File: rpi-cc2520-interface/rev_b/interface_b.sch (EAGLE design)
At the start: 5 parts, among them J1 PINHD-2X12/SMD, J2 PINHD-2X12/SMD

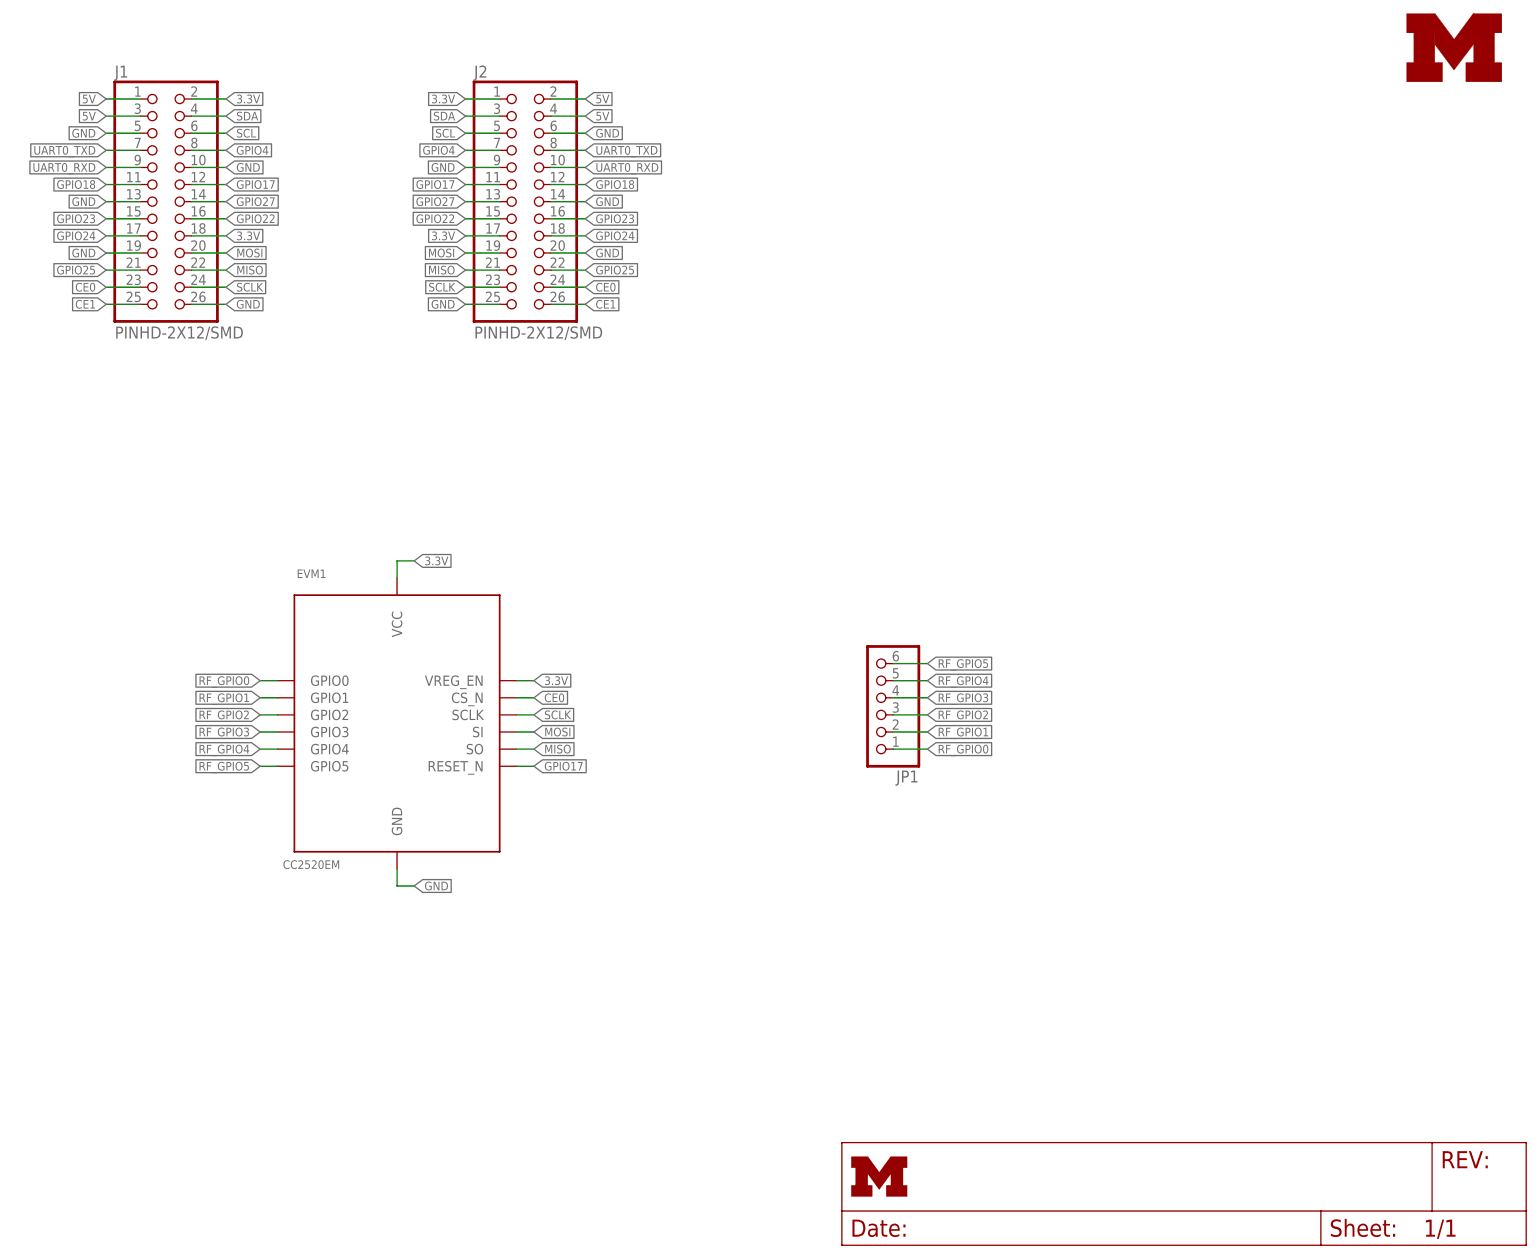
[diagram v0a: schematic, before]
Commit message: new rpi-cc2520 board is routed. want to add pin labels
git-svn-id: svn+ssh://energy.eecs.umich.edu/svnroot/shed/projects/pi-router/eagle@2756 d5a83394-2863-40c7-9603-03341d4c7fdc
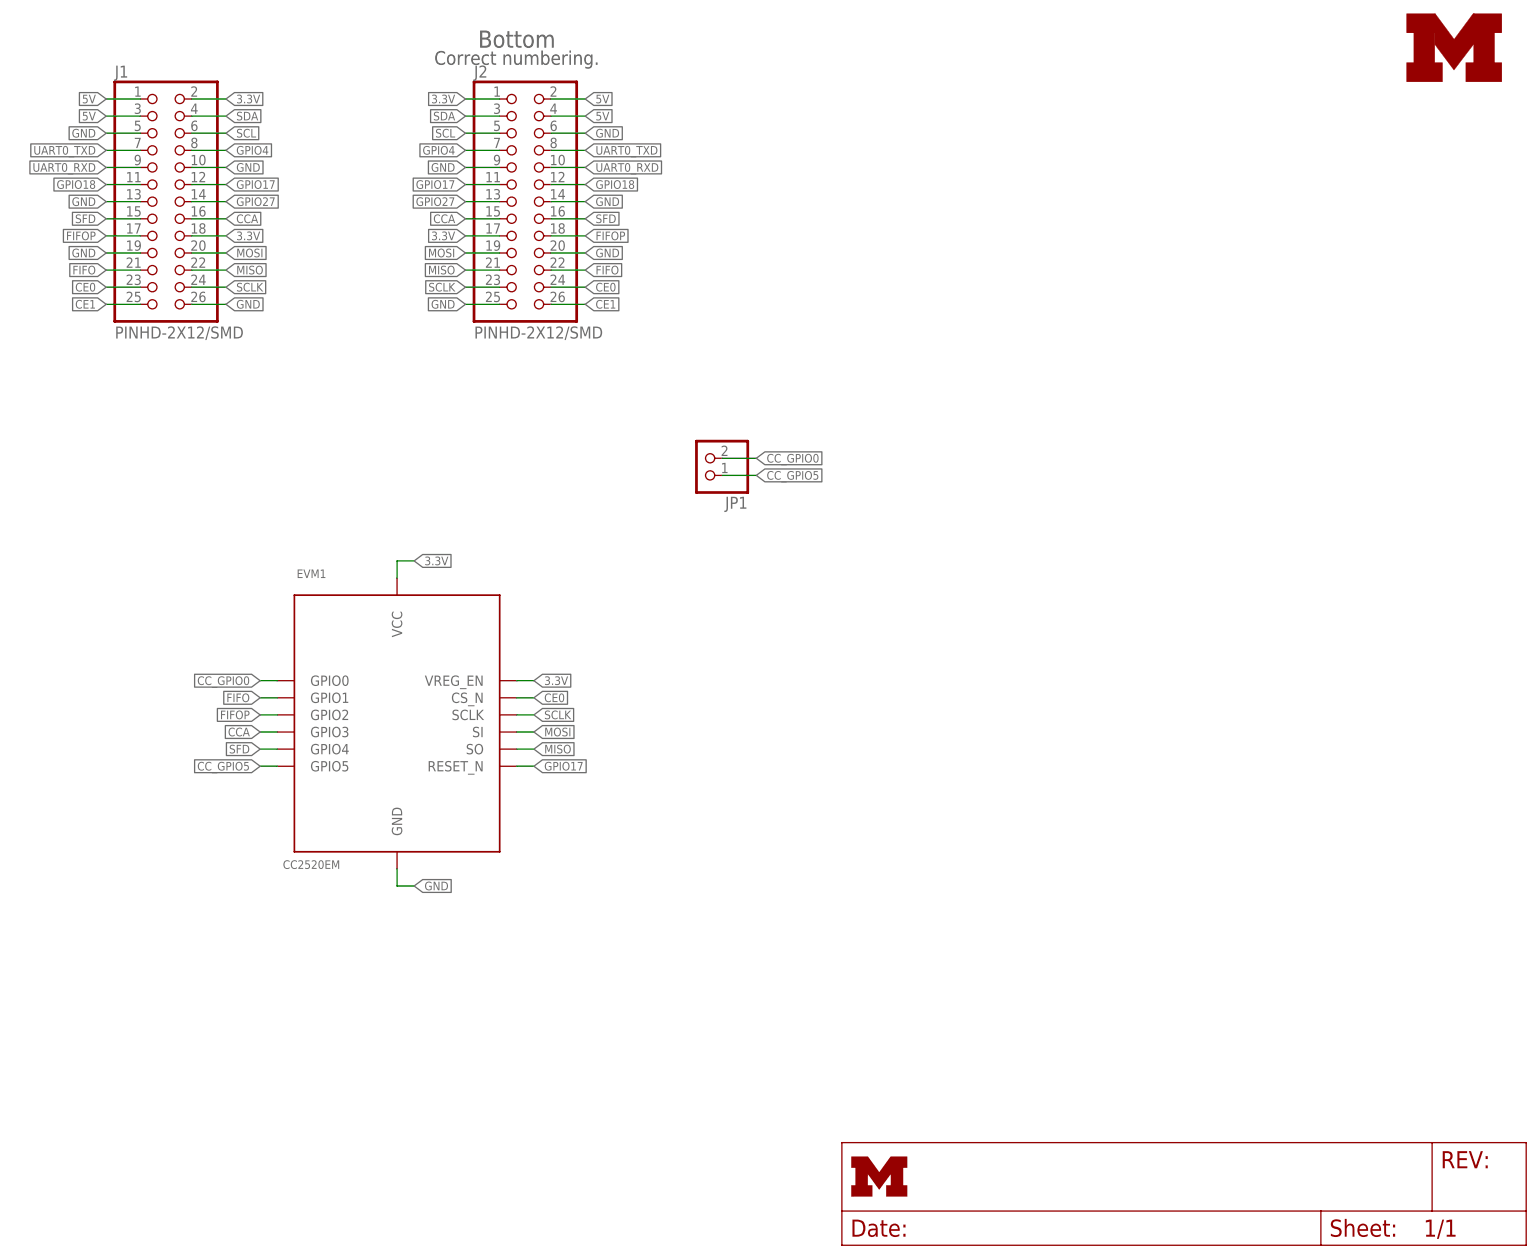
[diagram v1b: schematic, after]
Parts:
- JP1: device pinhead:PINHD-1X6/90 -> pinhead:PINHD-1X2
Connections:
- removed net GPIO22: J1.16, J2.15
- removed net GPIO23: J1.15, J2.16
- removed net GPIO24: J1.17, J2.18
- removed net GPIO25: J1.21, J2.22
- removed net RF_GPIO0: EVM1.GPIO0, JP1.1
- removed net RF_GPIO1: EVM1.GPIO1, JP1.2
- removed net RF_GPIO2: EVM1.GPIO2, JP1.3
- removed net RF_GPIO3: EVM1.GPIO3, JP1.4
- removed net RF_GPIO4: EVM1.GPIO4, JP1.5
- removed net RF_GPIO5: EVM1.GPIO5, JP1.6
- new net CCA: EVM1.GPIO3, J1.16, J2.15
- new net CC_GPIO0: EVM1.GPIO0, JP1.2
- new net CC_GPIO5: EVM1.GPIO5, JP1.1
- new net FIFO: EVM1.GPIO1, J1.21, J2.22
- new net FIFOP: EVM1.GPIO2, J1.17, J2.18
- new net SFD: EVM1.GPIO4, J1.15, J2.16
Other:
- note added: "Bottom"
- note added: "Correct numbering."
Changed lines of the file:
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@@
 <part name="J2" library="headers" deviceset="PINHD-2X12/SMD" device=""/>
 <part name="EVM1" library="brouter" deviceset="CC2520EM" device=""/>
-<part name="JP1" library="pinhead" deviceset="PINHD-1X6" device="/90"/>
+<part name="JP1" library="pinhead" deviceset="PINHD-1X2" device=""/>
 </parts>
 <sheets>
 <sheet>
 <plain>
+<text x="99.06" y="177.8" size="2.54" layer="97" align="bottom-center">Bottom</text>
+<text x="99.06" y="175.26" size="2.032" layer="97" align="bottom-center">Correct numbering.</text>
 </plain>
 <instances>
@@
 <instance part="J2" gate="G$1" x="99.06" y="154.94"/>
 <instance part="EVM1" gate="G$1" x="81.28" y="76.2"/>
-<instance part="JP1" gate="A" x="152.4" y="81.28" rot="R180"/>
+<instance part="JP1" gate="G$1" x="127" y="116.84" rot="R180"/>
 </instances>
 <busses>
@@
 </segment>
 </net>
-<net name="GPIO23" class="0">
-<segment>
-<pinref part="J1" gate="G$1" pin="15"/>
-<wire x1="43.18" y1="152.4" x2="38.1" y2="152.4" width="0.1524" layer="91"/>
-<label x="38.1" y="152.4" size="1.27" layer="95" rot="R180" xref="yes"/>
-</segment>
-<segment>
-<pinref part="J2" gate="G$1" pin="16"/>
-<wire x1="109.22" y1="152.4" x2="104.14" y2="152.4" width="0.1524" layer="91"/>
-<label x="109.22" y="152.4" size="1.27" layer="95" xref="yes"/>
-</segment>
-</net>
-<net name="GPIO24" class="0">
-<segment>
-<pinref part="J1" gate="G$1" pin="17"/>
-<wire x1="43.18" y1="149.86" x2="38.1" y2="149.86" width="0.1524" layer="91"/>
-<label x="38.1" y="149.86" size="1.27" layer="95" rot="R180" xref="yes"/>
-</segment>
-<segment>
-<pinref part="J2" gate="G$1" pin="18"/>
-<wire x1="109.22" y1="149.86" x2="104.14" y2="149.86" width="0.1524" layer="91"/>
-<label x="109.22" y="149.86" size="1.27" layer="95" xref="yes"/>
-</segment>
-</net>
-<net name="GPIO25" class="0">
-<segment>
-<pinref part="J1" gate="G$1" pin="21"/>
-<wire x1="43.18" y1="144.78" x2="38.1" y2="144.78" width="0.1524" layer="91"/>
-<label x="38.1" y="144.78" size="1.27" layer="95" rot="R180" xref="yes"/>
-</segment>
-<segment>
-<pinref part="J2" gate="G$1" pin="22"/>
-<wire x1="109.22" y1="144.78" x2="104.14" y2="144.78" width="0.1524" layer="91"/>
-<label x="109.22" y="144.78" size="1.27" layer="95" xref="yes"/>
-</segment>
-</net>
 <net name="CE0" class="0">
 <segment>
@@
 </segment>
 </net>
-<net name="GPIO22" class="0">
-<segment>
-<pinref part="J1" gate="G$1" pin="16"/>
-<wire x1="50.8" y1="152.4" x2="55.88" y2="152.4" width="0.1524" layer="91"/>
-<label x="55.88" y="152.4" size="1.27" layer="95" xref="yes"/>
-</segment>
-<segment>
-<pinref part="J2" gate="G$1" pin="15"/>
-<wire x1="96.52" y1="152.4" x2="91.44" y2="152.4" width="0.1524" layer="91"/>
-<label x="91.44" y="152.4" size="1.27" layer="95" rot="R180" xref="yes"/>
-</segment>
-</net>
 <net name="MOSI" class="0">
 <segment>
@@
 </segment>
 </net>
-<net name="RF_GPIO0" class="0">
+<net name="FIFO" class="0">
+<segment>
+<pinref part="EVM1" gate="G$1" pin="GPIO1"/>
+<wire x1="63.5" y1="81.28" x2="60.96" y2="81.28" width="0.1524" layer="91"/>
+<label x="60.96" y="81.28" size="1.27" layer="95" rot="R180" xref="yes"/>
+</segment>
+<segment>
+<pinref part="J2" gate="G$1" pin="22"/>
+<wire x1="109.22" y1="144.78" x2="104.14" y2="144.78" width="0.1524" layer="91"/>
+<label x="109.22" y="144.78" size="1.27" layer="95" xref="yes"/>
+</segment>
+<segment>
+<pinref part="J1" gate="G$1" pin="21"/>
+<wire x1="43.18" y1="144.78" x2="38.1" y2="144.78" width="0.1524" layer="91"/>
+<label x="38.1" y="144.78" size="1.27" layer="95" rot="R180" xref="yes"/>
+</segment>
+</net>
+<net name="FIFOP" class="0">
+<segment>
+<pinref part="EVM1" gate="G$1" pin="GPIO2"/>
+<wire x1="63.5" y1="78.74" x2="60.96" y2="78.74" width="0.1524" layer="91"/>
+<label x="60.96" y="78.74" size="1.27" layer="95" rot="R180" xref="yes"/>
+</segment>
+<segment>
+<pinref part="J2" gate="G$1" pin="18"/>
+<wire x1="109.22" y1="149.86" x2="104.14" y2="149.86" width="0.1524" layer="91"/>
+<label x="109.22" y="149.86" size="1.27" layer="95" xref="yes"/>
+</segment>
+<segment>
+<pinref part="J1" gate="G$1" pin="17"/>
+<wire x1="43.18" y1="149.86" x2="38.1" y2="149.86" width="0.1524" layer="91"/>
+<label x="38.1" y="149.86" size="1.27" layer="95" rot="R180" xref="yes"/>
+</segment>
+</net>
+<net name="CCA" class="0">
+<segment>
+<pinref part="EVM1" gate="G$1" pin="GPIO3"/>
+<wire x1="63.5" y1="76.2" x2="60.96" y2="76.2" width="0.1524" layer="91"/>
+<label x="60.96" y="76.2" size="1.27" layer="95" rot="R180" xref="yes"/>
+</segment>
+<segment>
+<pinref part="J2" gate="G$1" pin="15"/>
+<wire x1="96.52" y1="152.4" x2="91.44" y2="152.4" width="0.1524" layer="91"/>
+<label x="91.44" y="152.4" size="1.27" layer="95" rot="R180" xref="yes"/>
+</segment>
+<segment>
+<pinref part="J1" gate="G$1" pin="16"/>
+<wire x1="50.8" y1="152.4" x2="55.88" y2="152.4" width="0.1524" layer="91"/>
+<label x="55.88" y="152.4" size="1.27" layer="95" xref="yes"/>
+</segment>
+</net>
+<net name="SFD" class="0">
+<segment>
+<pinref part="EVM1" gate="G$1" pin="GPIO4"/>
+<wire x1="63.5" y1="73.66" x2="60.96" y2="73.66" width="0.1524" layer="91"/>
+<label x="60.96" y="73.66" size="1.27" layer="95" rot="R180" xref="yes"/>
+</segment>
+<segment>
+<pinref part="J2" gate="G$1" pin="16"/>
+<wire x1="109.22" y1="152.4" x2="104.14" y2="152.4" width="0.1524" layer="91"/>
+<label x="109.22" y="152.4" size="1.27" layer="95" xref="yes"/>
+</segment>
+<segment>
+<pinref part="J1" gate="G$1" pin="15"/>
+<wire x1="43.18" y1="152.4" x2="38.1" y2="152.4" width="0.1524" layer="91"/>
+<label x="38.1" y="152.4" size="1.27" layer="95" rot="R180" xref="yes"/>
+</segment>
+</net>
+<net name="CC_GPIO5" class="0">
+<segment>
+<pinref part="EVM1" gate="G$1" pin="GPIO5"/>
+<wire x1="63.5" y1="71.12" x2="60.96" y2="71.12" width="0.1524" layer="91"/>
+<label x="60.96" y="71.12" size="1.27" layer="95" rot="R180" xref="yes"/>
+</segment>
+<segment>
+<pinref part="JP1" gate="G$1" pin="1"/>
+<wire x1="129.54" y1="114.3" x2="134.62" y2="114.3" width="0.1524" layer="91"/>
+<label x="134.62" y="114.3" size="1.27" layer="95" xref="yes"/>
+</segment>
+</net>
+<net name="CC_GPIO0" class="0">
 <segment>
 <pinref part="EVM1" gate="G$1" pin="GPIO0"/>
@@
 </segment>
 <segment>
-<pinref part="JP1" gate="A" pin="1"/>
-<wire x1="160.02" y1="73.66" x2="154.94" y2="73.66" width="0.1524" layer="91"/>
-<label x="160.02" y="73.66" size="1.27" layer="95" xref="yes"/>
-</segment>
-</net>
-<net name="RF_GPIO1" class="0">
-<segment>
-<pinref part="EVM1" gate="G$1" pin="GPIO1"/>
-<wire x1="60.96" y1="81.28" x2="63.5" y2="81.28" width="0.1524" layer="91"/>
-<label x="60.96" y="81.28" size="1.27" layer="95" rot="R180" xref="yes"/>
-</segment>
-<segment>
-<pinref part="JP1" gate="A" pin="2"/>
-<wire x1="160.02" y1="76.2" x2="154.94" y2="76.2" width="0.1524" layer="91"/>
-<label x="160.02" y="76.2" size="1.27" layer="95" xref="yes"/>
-</segment>
-</net>
-<net name="RF_GPIO2" class="0">
-<segment>
-<pinref part="EVM1" gate="G$1" pin="GPIO2"/>
-<wire x1="60.96" y1="78.74" x2="63.5" y2="78.74" width="0.1524" layer="91"/>
-<label x="60.96" y="78.74" size="1.27" layer="95" rot="R180" xref="yes"/>
-</segment>
-<segment>
-<pinref part="JP1" gate="A" pin="3"/>
-<wire x1="160.02" y1="78.74" x2="154.94" y2="78.74" width="0.1524" layer="91"/>
-<label x="160.02" y="78.74" size="1.27" layer="95" xref="yes"/>
-</segment>
-</net>
-<net name="RF_GPIO3" class="0">
-<segment>
-<pinref part="EVM1" gate="G$1" pin="GPIO3"/>
-<wire x1="60.96" y1="76.2" x2="63.5" y2="76.2" width="0.1524" layer="91"/>
-<label x="60.96" y="76.2" size="1.27" layer="95" rot="R180" xref="yes"/>
-</segment>
-<segment>
-<pinref part="JP1" gate="A" pin="4"/>
-<wire x1="160.02" y1="81.28" x2="154.94" y2="81.28" width="0.1524" layer="91"/>
-<label x="160.02" y="81.28" size="1.27" layer="95" xref="yes"/>
-</segment>
-</net>
-<net name="RF_GPIO4" class="0">
-<segment>
-<pinref part="EVM1" gate="G$1" pin="GPIO4"/>
-<wire x1="60.96" y1="73.66" x2="63.5" y2="73.66" width="0.1524" layer="91"/>
-<label x="60.96" y="73.66" size="1.27" layer="95" rot="R180" xref="yes"/>
-</segment>
-<segment>
-<pinref part="JP1" gate="A" pin="5"/>
-<wire x1="160.02" y1="83.82" x2="154.94" y2="83.82" width="0.1524" layer="91"/>
-<label x="160.02" y="83.82" size="1.27" layer="95" xref="yes"/>
-</segment>
-</net>
-<net name="RF_GPIO5" class="0">
-<segment>
-<pinref part="EVM1" gate="G$1" pin="GPIO5"/>
-<wire x1="60.96" y1="71.12" x2="63.5" y2="71.12" width="0.1524" layer="91"/>
-<label x="60.96" y="71.12" size="1.27" layer="95" rot="R180" xref="yes"/>
-</segment>
-<segment>
-<pinref part="JP1" gate="A" pin="6"/>
-<wire x1="160.02" y1="86.36" x2="154.94" y2="86.36" width="0.1524" layer="91"/>
-<label x="160.02" y="86.36" size="1.27" layer="95" xref="yes"/>
-</segment>
-</net>
+<pinref part="JP1" gate="G$1" pin="2"/>
+<wire x1="129.54" y1="116.84" x2="134.62" y2="116.84" width="0.1524" layer="91"/>
+<label x="134.62" y="116.84" size="1.27" layer="95" xref="yes"/>
+</segment>
+</net>

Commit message: added LEDS and pin labels to interface board
git-svn-id: svn+ssh://energy.eecs.umich.edu/svnroot/shed/projects/pi-router/eagle@2765 d5a83394-2863-40c7-9603-03341d4c7fdc
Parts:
- added D1, D2, D3: (no value), SparkFun-LED:LED0603
- added R1, R2, R3: (no value), rcl:R-US_R0603
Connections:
- removed net 3.3V: EVM1.VCC, EVM1.VREG_EN, J1.18, J1.2, J2.1, J2.17
- removed net GPIO18: J1.11, J2.12
- removed net GPIO27: J1.14, J2.13
- removed net GPIO4: J1.8, J2.7
- new net LED0: J1.8, J2.7, R1.1
- new net LED1: J1.11, J2.12, R2.1
- new net LED2: J1.14, J2.13, R3.1
- new net N$1: D1.C, R1.2
- new net N$2: D2.C, R2.2
- new net N$3: D3.C, R3.2
- new net VCC: D1.A, D2.A, D3.A, EVM1.VCC, EVM1.VREG_EN, J1.18, J1.2, J2.1, J2.17
